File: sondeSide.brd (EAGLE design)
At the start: 66.8 x 32 mm, 32 parts

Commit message: Before adding the remote board
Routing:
- net 3.3V: track 64.5 -> 76.4 mm
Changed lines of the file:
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@@
 <wire x1="36.322" y1="24.892" x2="43.688" y2="24.892" width="0.3048" layer="16"/>
 <wire x1="36.322" y1="24.892" x2="35.052" y2="26.162" width="0.3048" layer="16"/>
-<wire x1="48.514" y1="10.922" x2="46.99" y2="12.446" width="0.8128" layer="16"/>
-<wire x1="46.99" y1="12.446" x2="41.402" y2="12.446" width="0.8128" layer="16"/>
-<wire x1="41.402" y1="12.446" x2="41.402" y2="14.986" width="0.8128" layer="16"/>
-<wire x1="41.402" y1="12.446" x2="41.402" y2="11.557" width="0.8128" layer="16"/>
-<wire x1="41.402" y1="11.557" x2="40.767" y2="10.922" width="0.8128" layer="16"/>
 <wire x1="23.368" y1="24.638" x2="23.368" y2="19.304" width="1.524" layer="16"/>
 <wire x1="10.16" y1="28.448" x2="10.16" y2="29.972" width="1.524" layer="16"/>
@@
 <wire x1="25.4" y1="17.272" x2="37.084" y2="17.272" width="1.524" layer="16"/>
 <wire x1="37.084" y1="17.272" x2="39.37" y2="14.986" width="1.524" layer="16"/>
-<wire x1="37.084" y1="17.272" x2="36.322" y2="24.892" width="0" layer="19" extent="16-16"/>
+<wire x1="35.052" y1="26.162" x2="24.892" y2="26.162" width="0.3048" layer="16"/>
+<wire x1="24.892" y1="26.162" x2="23.368" y2="24.638" width="0.3048" layer="16"/>
+<wire x1="41.402" y1="14.986" x2="41.402" y2="11.557" width="1.016" layer="16"/>
+<wire x1="41.402" y1="11.557" x2="40.767" y2="10.922" width="1.016" layer="16"/>
+<wire x1="41.402" y1="11.557" x2="47.879" y2="11.557" width="1.016" layer="16"/>
+<wire x1="47.879" y1="11.557" x2="48.514" y2="10.922" width="1.016" layer="16"/>
 </signal>
 <signal name="GND">
@@
 <contactref element="STEP-UP" pad="3"/>
 <contactref element="SONDE" pad="1"/>
-<wire x1="62.738" y1="25.4" x2="64.516" y2="23.622" width="0.508" layer="16"/>
-<wire x1="64.516" y1="23.622" x2="64.516" y2="7.493" width="0.508" layer="16"/>
+<wire x1="62.738" y1="25.4" x2="62.738" y2="10.668" width="1.27" layer="16"/>
+<wire x1="64.516" y1="8.89" x2="64.516" y2="7.493" width="1.27" layer="16"/>
+<wire x1="62.738" y1="10.668" x2="64.516" y2="8.89" width="1.27" layer="16"/>
 </signal>
 <signal name="SDA">

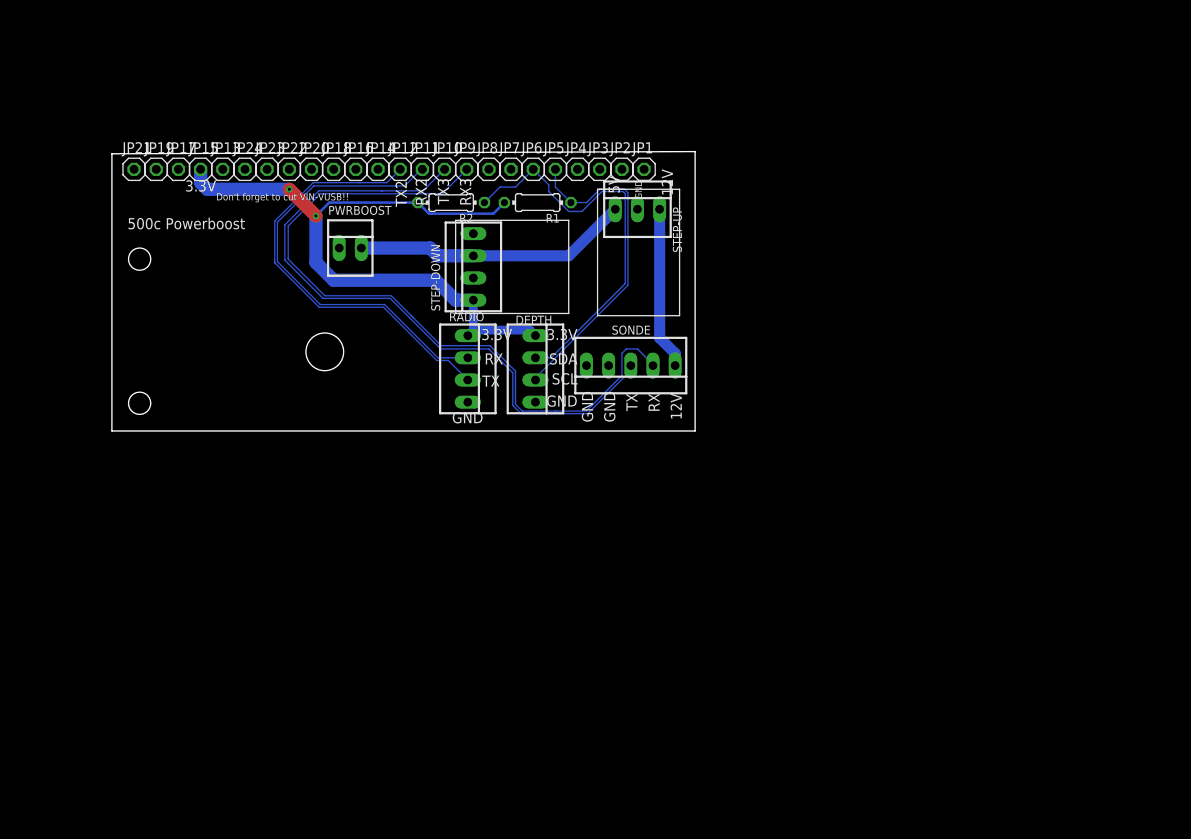
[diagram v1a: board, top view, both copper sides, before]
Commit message: Proposed layout, routing time
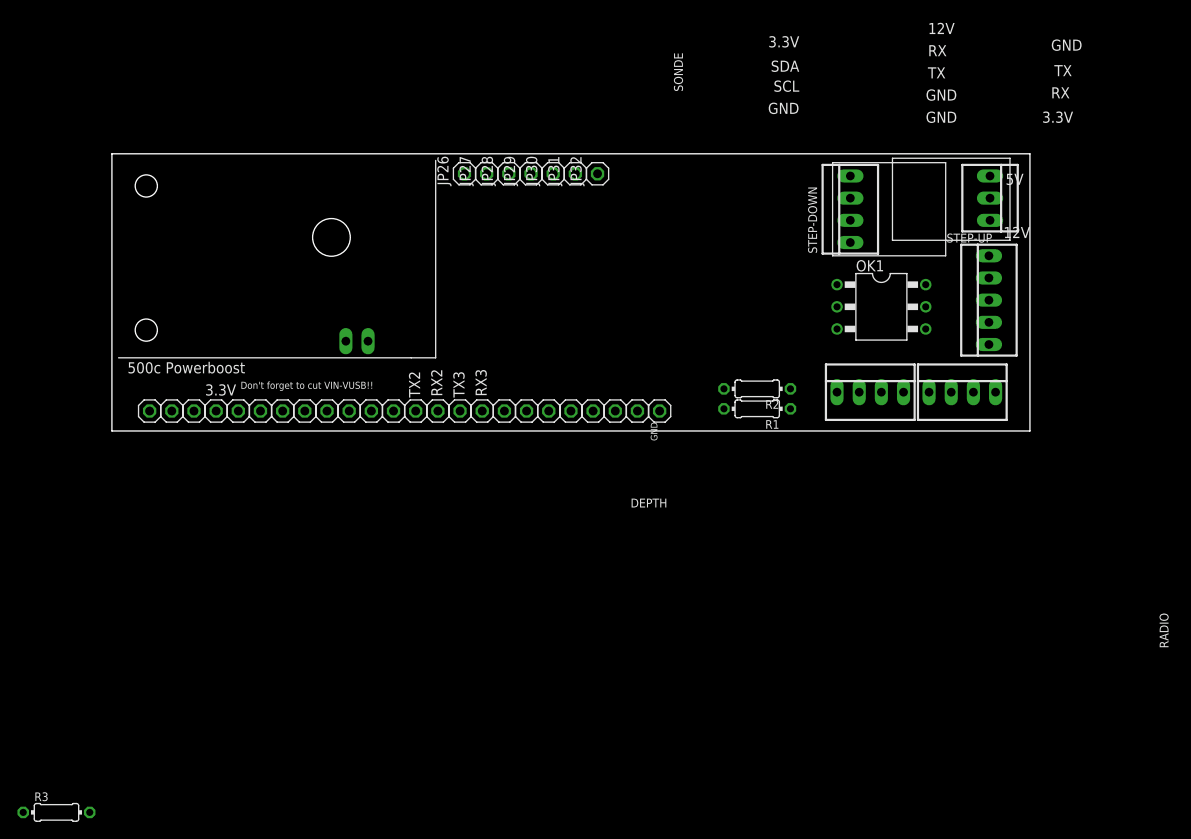
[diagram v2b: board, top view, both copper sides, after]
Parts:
- added JP26, JP27, JP28, JP29, JP30, JP31, JP32: (no value), pinhead:1X01
- added OK1: H11L2MT, optocoupler:DIL6-04
- added R3: (no value), rcl:0204/7
- R1, R2: value (none) -> 4.7k
- moved DEPTH 49.0 mm to (97.4, 4.45), turned to 0 degrees
- moved RADIO 46.2 mm to (86.9, 4.45), turned to 0 degrees
- moved STEP-DOWN 43.7 mm to (84.6, 25.4)
- moved SONDE 41.7 mm to (100.5, 15.0), turned to 90 degrees
- moved R2 41.0 mm to (73.9, 4.83)
- moved STEP-UP 40.4 mm to (100.6, 26.7), turned to 270 degrees
- moved R1 34.5 mm to (73.9, 2.54)
- moved JP1 27.7 mm to (62.7, 2.29)
- moved JP10 27.7 mm to (39.9, 2.29)
- moved JP11 27.7 mm to (37.3, 2.29)
- moved JP12 27.7 mm to (34.8, 2.29)
- moved JP13 27.7 mm to (14.5, 2.29)
- moved JP14 27.7 mm to (32.3, 2.29)
- moved JP15 27.7 mm to (11.9, 2.29)
- moved JP16 27.7 mm to (29.7, 2.29)
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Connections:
- new net D0: JP28.1
- new net D1: JP29.1, R3.2
- new net D2: JP30.1
- new net D3: JP31.1
- new net GND_PLANE: JP26.1, OK1.2, OK1.5
- new net N$1: OK1.1, R3.1
- new net VT: JP32.1
- net 5V: now also JP27.1
- net GND: now also OK1.4, OK1.6
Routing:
- net RX3: track 83.8 -> 0.00 mm
- net TX3: track 76.9 -> 0.00 mm
- net 3.3V: track 76.4 -> 0.00 mm, vias 2 -> 0
- net RX2: track 50.0 -> 0.00 mm
- net TX2: track 49.6 -> 0.00 mm
- net SDA: track 45.3 -> 0.00 mm
- net SCL: track 37.8 -> 0.00 mm
- net 5V: track 31.7 -> 0.00 mm
- net 12V: track 18.6 -> 0.00 mm
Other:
- board size 66.8 x 32 mm -> 105.2 x 31.8 mm

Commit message: About to do significant rerouting
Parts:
- moved R3 106.2 mm to (82.8, 14.0), turned to 270 degrees
- moved R1 7.23 mm to (67.1, 4.83), turned to 0 degrees
- moved OK1 2.54 mm to (90.7, 14.2)
- moved R2 2.29 mm to (76.2, 4.83)
- moved RADIO 0.51 mm to (86.9, 4.95)
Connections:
- net GND: no longer PWRBOOST.1
- net GND_PLANE: now also PWRBOOST.1
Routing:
- net 3.3V: track 0.00 -> 116.4 mm
- net 5V: track 0.00 -> 83.6 mm
- net GND: track 0.00 -> 57.6 mm
- net N$1: track 0.00 -> 3.21 mm

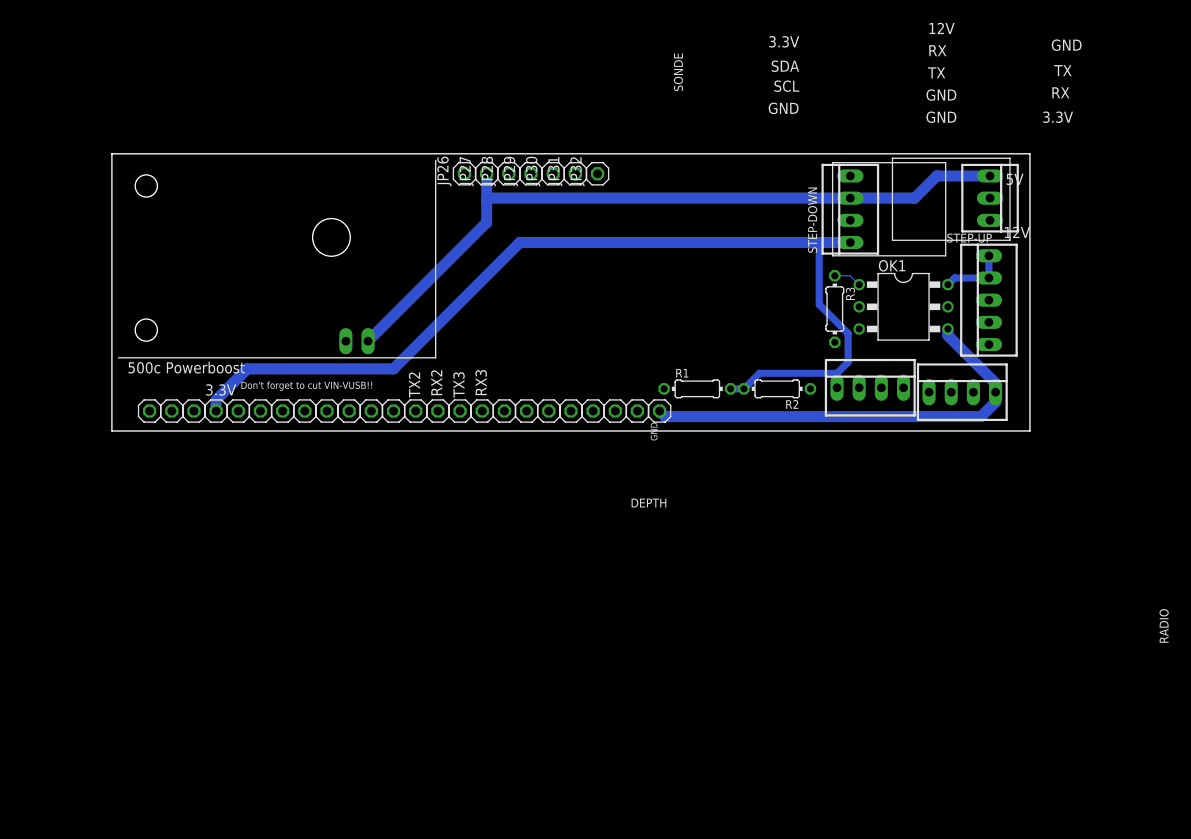
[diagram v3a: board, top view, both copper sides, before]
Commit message: If we can swap the serial ports, good to go
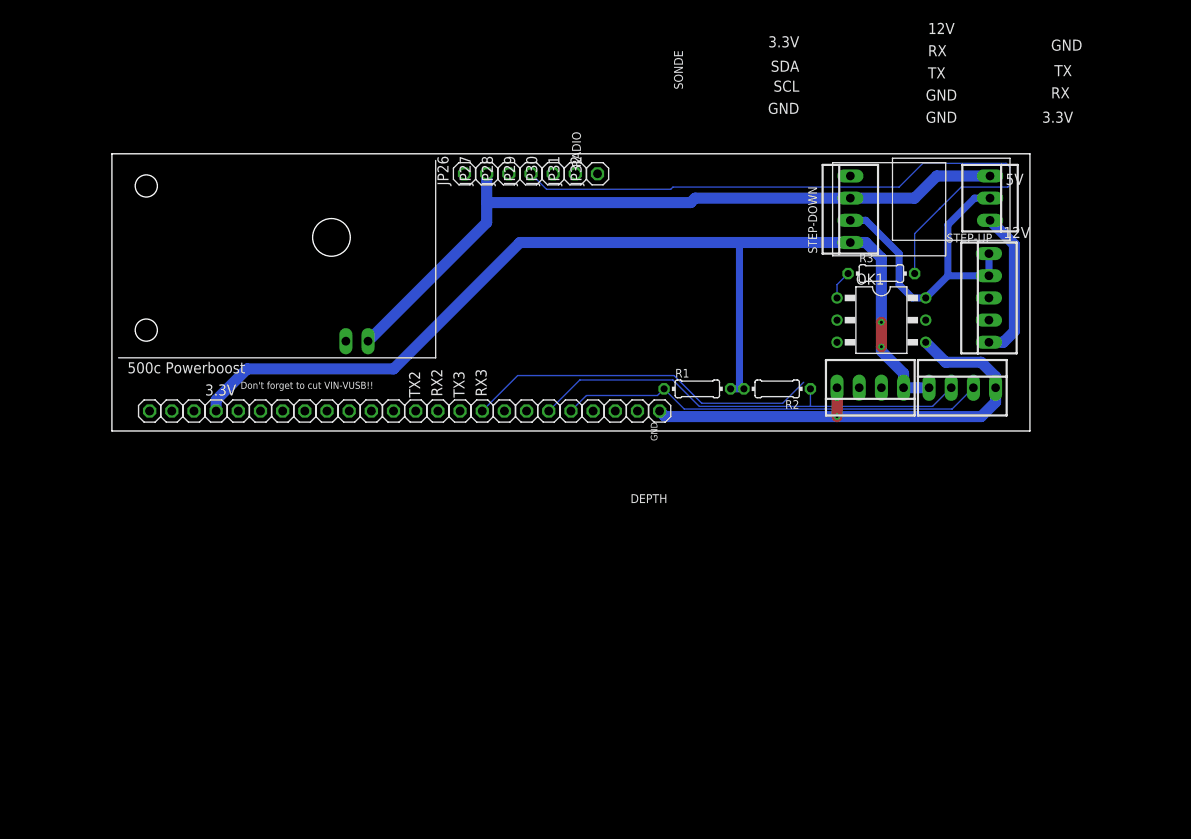
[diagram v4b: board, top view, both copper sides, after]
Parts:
- moved R3 6.71 mm to (88.1, 18.0), turned to 0 degrees
- moved OK1 2.96 mm to (88.1, 12.7)
- moved DEPTH 0.51 mm to (97.4, 4.95)
- moved SONDE 0.25 mm to (100.5, 15.2)
- turned RADIO to 180 degrees
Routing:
- net D1: track 0.00 -> 77.0 mm
- net SDA: track 0.00 -> 51.7 mm
- net SCL: track 0.00 -> 49.1 mm
- net RX3: track 0.00 -> 40.8 mm
- net GND: track 57.6 -> 93.0 mm, vias 0 -> 1
- net 12V: track 0.00 -> 17.3 mm
- net 3.3V: track 116.4 -> 126.7 mm, vias 0 -> 2

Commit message: Good to go! Just place labels
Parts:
- moved R1 0.51 mm to (67.1, 5.33)
- moved R2 0.51 mm to (76.2, 5.33)
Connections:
- net RX2: now also SONDE.2; no longer RADIO.2
- net RX3: now also RADIO.2; no longer SONDE.2
- net TX2: now also SONDE.3; no longer RADIO.3
- net TX3: now also RADIO.3; no longer SONDE.3
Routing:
- net TX2: track 0.00 -> 74.4 mm
- net RX2: track 0.00 -> 70.8 mm
- net TX3: track 0.00 -> 52.0 mm
- net RX3: track 40.8 -> 54.3 mm
- net SDA: track 51.7 -> 52.6 mm
- net 3.3V: track 126.7 -> 125.9 mm
- net D1: track 77.0 -> 76.4 mm

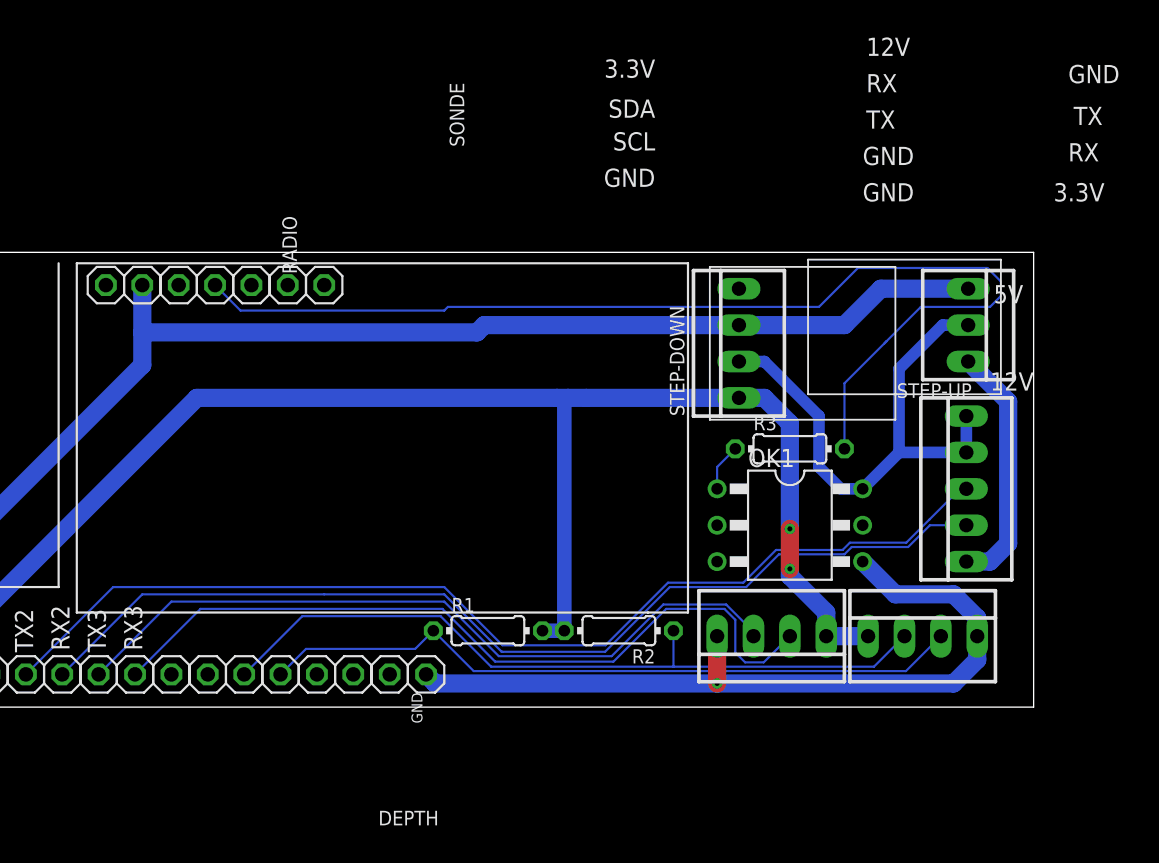
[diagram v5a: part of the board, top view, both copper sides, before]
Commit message: Flipped sonde connector
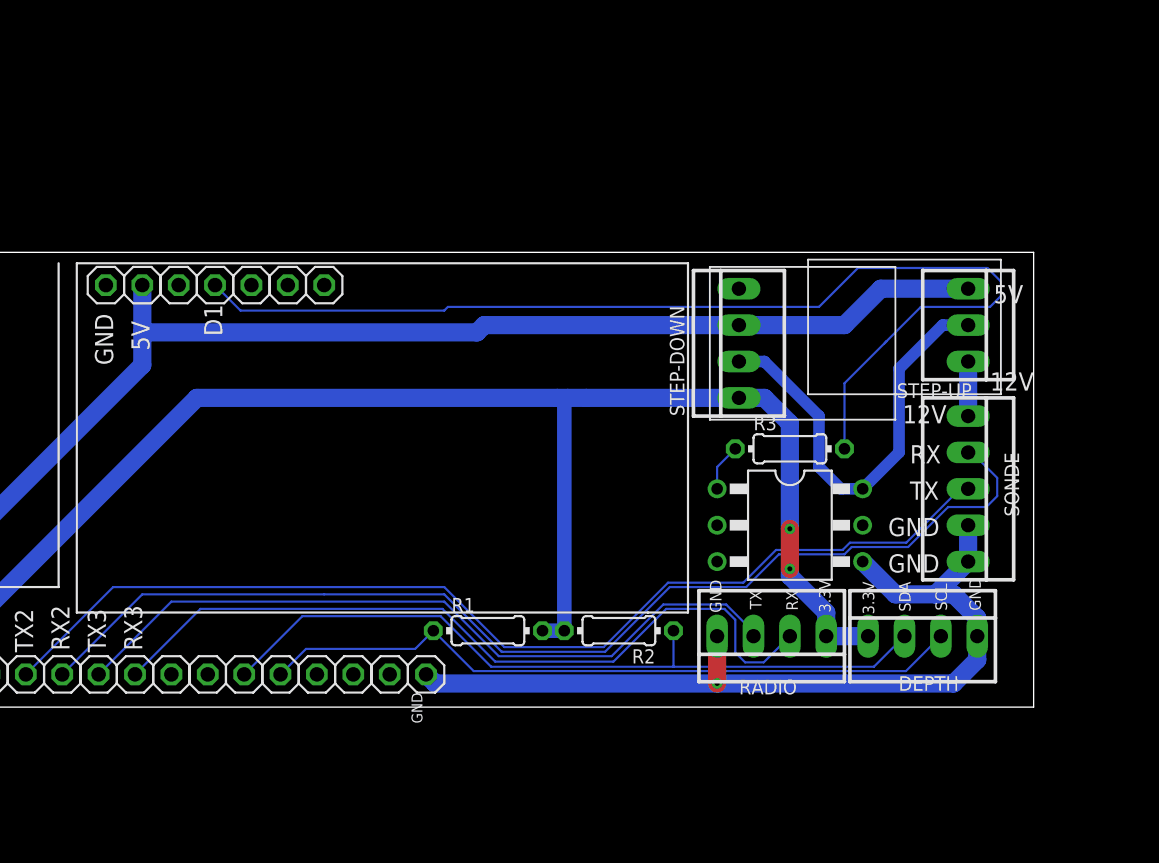
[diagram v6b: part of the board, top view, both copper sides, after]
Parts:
- moved SONDE 0.13 mm to (100.6, 15.2), turned to 270 degrees
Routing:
- net 12V: track 17.3 -> 3.81 mm
- net RX2: track 70.8 -> 77.8 mm
- net GND: track 93.0 -> 91.5 mm
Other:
- board text added: "D1"

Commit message: Board is good to go
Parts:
- R3: value (none) -> 370Ω
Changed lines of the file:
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@@
 <text x="58.166" y="22.86" size="1.27" layer="26" rot="MR270">5V</text>
 <text x="60.96" y="22.86" size="1.27" layer="26" rot="MR270">GND</text>
-<text x="61.722" y="1.016" size="0.762" layer="25" rot="R270">GND</text>
+<text x="64.008" y="2.032" size="0.762" layer="25">GND</text>
 <text x="102.108" y="22.098" size="1.27" layer="25">12V</text>
 <text x="63.5" y="22.86" size="1.27" layer="26" rot="MR270">12V</text>
@@
 <attribute name="OC_NEWARK" value="unknown" x="88.138" y="12.7" size="1.778" layer="27" rot="R270" display="off"/>
 </element>
-<element name="R3" library="rcl" library_urn="urn:adsk.eagle:library:334" package="0204/7" package3d_urn="urn:adsk.eagle:package:23498/1" value="" x="88.138" y="18.034">
+<element name="R3" library="rcl" library_urn="urn:adsk.eagle:library:334" package="0204/7" package3d_urn="urn:adsk.eagle:package:23498/1" value="370Ω" x="88.138" y="18.034">
 <attribute name="SPICEPREFIX" value="R" x="88.138" y="18.034" size="1.778" layer="27" display="off"/>
 </element>
